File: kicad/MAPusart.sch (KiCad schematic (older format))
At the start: 9 parts, among them J3 USB-Micro, U3 CP210X

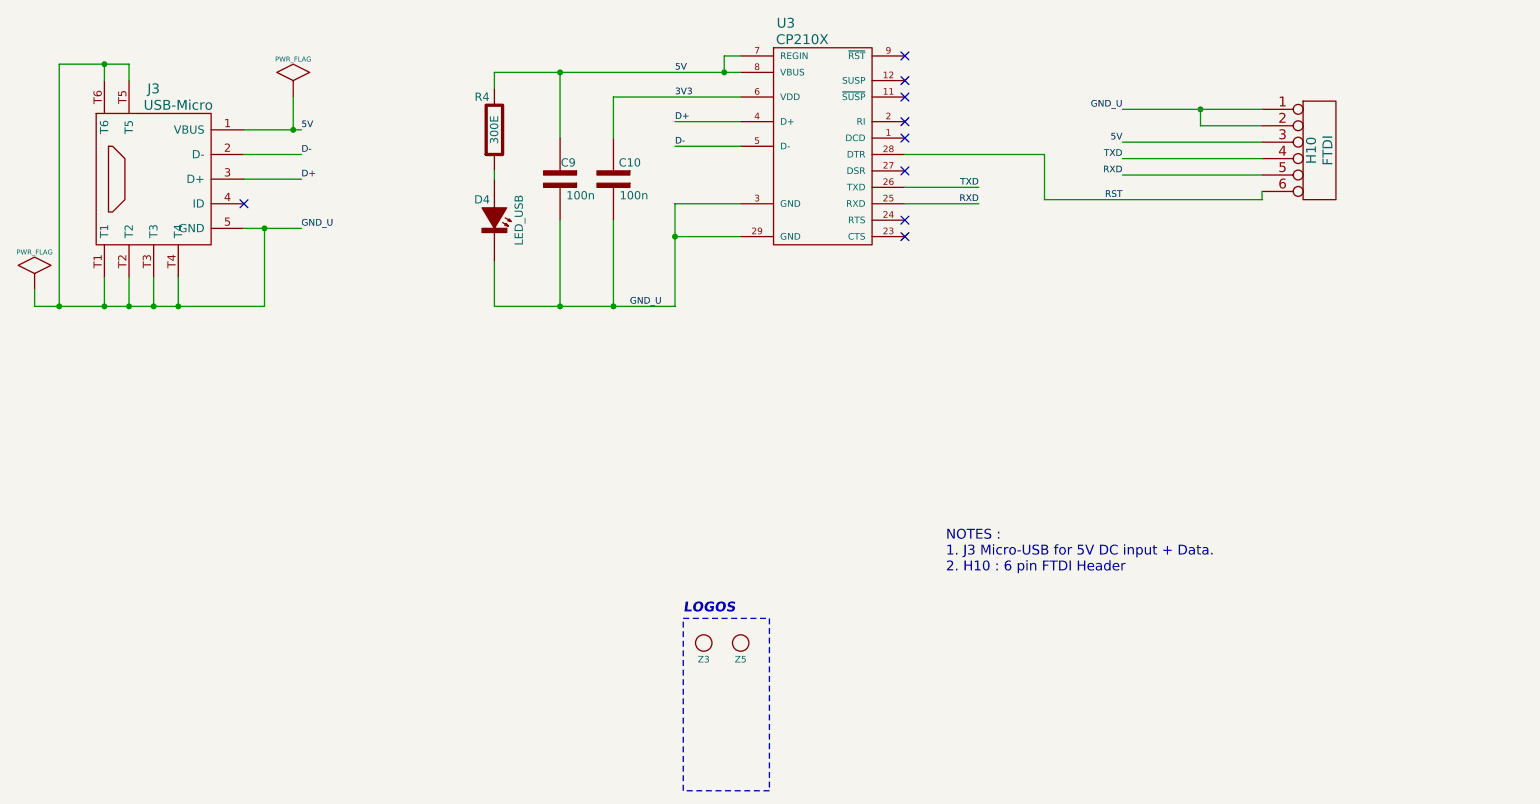
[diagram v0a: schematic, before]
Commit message: MAPusart schematic, PCB complete. Bom pending
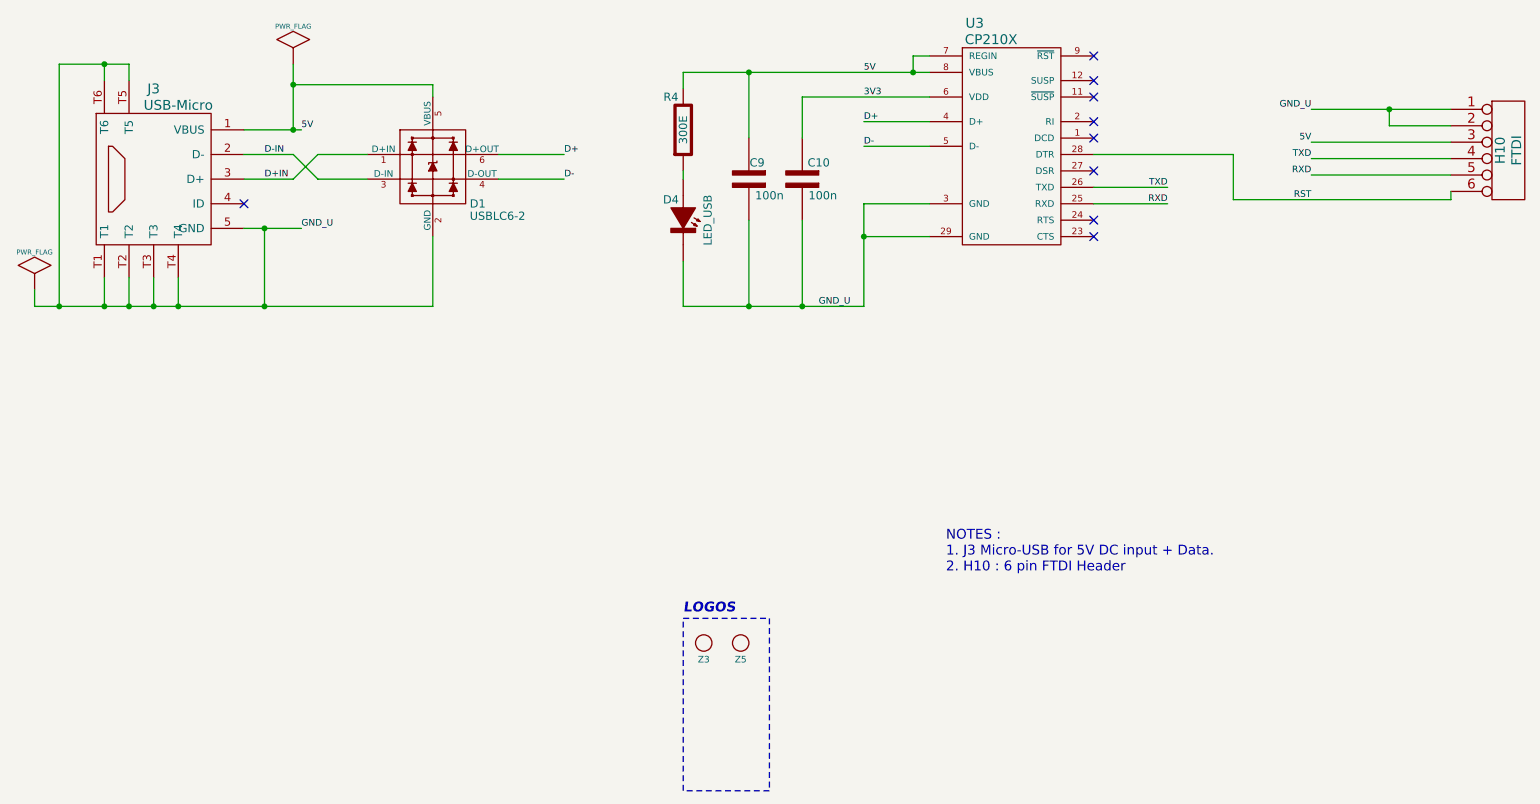
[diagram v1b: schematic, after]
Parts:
- added D1: USBLC6-2, MAPusart.pretty:SOT-23-6, symbol USBLC6-2
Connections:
- net 5V: now also D1.5 (VBUS)
- net D+: now also D1.6 (D+OUT); no longer J3.3 (D+)
- net D-: now also D1.4 (D-OUT); no longer J3.2 (D-)
- net GND_U: now also D1.2 (GND)
- new net D+IN: D1.1 (D+IN), J3.3 (D+)
- new net D-IN: D1.3 (D-IN), J3.2 (D-)
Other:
- moved on the sheet: C10, C9, D4, H10, R4, U3

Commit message: MAPusart complete and ready for prototyping
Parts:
- C10, C9: footprint MAPone.pretty:C_0805_HandSoldering -> MAPusart.pretty:C_0805_HandSoldering
- D4: footprint MAPone.pretty:LED-0805 -> MAPusart.pretty:LED-0805
- H10: footprint MAPone.pretty:Socket_Strip_Angled_1x06 -> MAPusart.pretty:Socket_Strip_Angled_1x06
- J3: footprint MAPone.pretty:USB_B_Micro -> MAPusart.pretty:USB_B_Micro
- R4: footprint MAPone.pretty:R_0805_HandSoldering -> MAPusart.pretty:R_0805_HandSoldering
- U3: footprint MAPone.pretty:qfn-28 -> MAPusart.pretty:qfn-28
- Z5: footprint MAPusart:OSHW_6mm -> MAPusart.pretty:OSHW_6mm
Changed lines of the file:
@@
 F 0 "U3" H 7150 4325 60  0000 C CNN
 F 1 "CP210X" H 7250 4225 60  0000 C CNN
-F 2 "MAPone.pretty:qfn-28" H 7375 3775 60  0001 C CNN
+F 2 "MAPusart.pretty:qfn-28" H 7375 3775 60  0001 C CNN
 F 3 "" H 7375 3775 60  0000 C CNN
 	1    7375 3575
@@
 F 0 "J3" H 2150 4325 60  0000 C CNN
 F 1 "USB-Micro" H 2300 4225 60  0000 C CNN
-F 2 "MAPone.pretty:USB_B_Micro" H 2150 3775 60  0001 C CNN
+F 2 "MAPusart.pretty:USB_B_Micro" H 2150 3775 60  0001 C CNN
 F 3 "" H 2150 3775 60  0000 C CNN
 	1    2150 3775
@@
 F 0 "C10" V 6000 3875 50  0000 C CNN
 F 1 "100n" V 6200 3900 50  0000 C CNN
-F 2 "MAPone.pretty:C_0805_HandSoldering" H 6050 3775 60  0001 C CNN
+F 2 "MAPusart.pretty:C_0805_HandSoldering" H 6050 3775 60  0001 C CNN
 F 3 "" H 6050 3775 60  0000 C CNN
 	1    6100 3775
@@
 F 0 "C9" V 5675 3825 50  0000 C CNN
 F 1 "100n" V 5875 3900 50  0000 C CNN
-F 2 "MAPone.pretty:C_0805_HandSoldering" H 5725 3775 60  0001 C CNN
+F 2 "MAPusart.pretty:C_0805_HandSoldering" H 5725 3775 60  0001 C CNN
 F 3 "" H 5725 3775 60  0000 C CNN
 	1    5775 3775
@@
 F 0 "R4" V 5175 3400 50  0000 C CNN
 F 1 "300E" H 5375 3475 50  0000 C CNN
-F 2 "MAPone.pretty:R_0805_HandSoldering" H 5325 3475 60  0001 C CNN
+F 2 "MAPusart.pretty:R_0805_HandSoldering" H 5325 3475 60  0001 C CNN
 F 3 "" H 5325 3475 60  0000 C CNN
 	1    5375 3475
@@
 F 0 "D4" V 5250 3950 50  0000 C CNN
 F 1 "LED_USB" H 5375 4175 50  0000 C CNN
-F 2 "MAPone.pretty:LED-0805" H 5445 4025 60  0001 C CNN
+F 2 "MAPusart.pretty:LED-0805" H 5445 4025 60  0001 C CNN
 F 3 "" H 5445 4025 60  0000 C CNN
 	1    5375 4025
@@
 F 0 "H10" V 10350 3600 60  0000 C CNN
 F 1 "FTDI" V 10450 3600 60  0000 C CNN
-F 2 "MAPone.pretty:Socket_Strip_Angled_1x06" H 10400 3600 60  0001 C CNN
+F 2 "MAPusart.pretty:Socket_Strip_Angled_1x06" H 10400 3600 60  0001 C CNN
 F 3 "" H 10400 3600 60  0001 C CNN
 	1    10400 3600
@@
 F 0 "Z5" H 5725 6500 40  0000 C CNN
 F 1 "SCREW" H 5725 6700 40  0001 C CNN
-F 2 "MAPusart:OSHW_6mm" H 5725 6600 60  0001 C CNN
+F 2 "MAPusart.pretty:OSHW_6mm" H 5725 6600 60  0001 C CNN
 F 3 "" H 5725 6600 60  0000 C CNN
 	1    5725 6600
